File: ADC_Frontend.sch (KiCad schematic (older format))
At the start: 3 parts

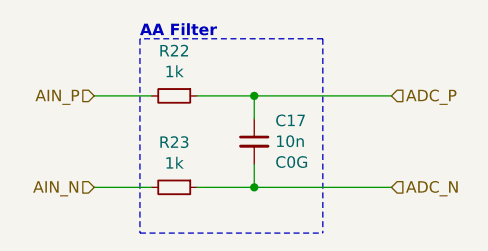
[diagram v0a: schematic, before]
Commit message: Change Sensor Connectors
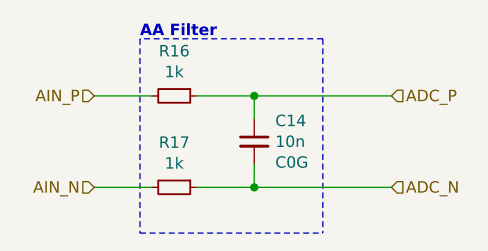
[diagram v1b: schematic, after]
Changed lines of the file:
@@
 $Descr A4 11693 8268
 encoding utf-8
-Sheet 6 17
+Sheet 3 17
 Title "Kleinvoet"
 Date "2020-06-11"
@@
 AR Path="/5EE5ECAD/5EE91C90/5EF8AB51" Ref="R20"  Part="1"
 AR Path="/5EE5ECAD/5EE9492B/5EF8AB51" Ref="R22"  Part="1"
-F 0 "R22" V 2854 2450 50  0000 C CNN
+F 0 "R16" V 2854 2450 50  0000 C CNN
 F 1 "1k" V 2945 2450 50  0000 C CNN
 F 2 "Resistor_SMD:R_0603_1608Metric_Pad1.05x0.95mm_HandSolder" H 3050 2450 50  0001 C CNN
@@
 AR Path="/5EE5ECAD/5EE91C90/5EF8AB5E" Ref="C16"  Part="1"
 AR Path="/5EE5ECAD/5EE9492B/5EF8AB5E" Ref="C17"  Part="1"
-F 0 "C17" H 3492 2741 50  0000 L CNN
+F 0 "C14" H 3492 2741 50  0000 L CNN
 F 1 "10n" H 3492 2650 50  0000 L CNN
 F 2 "Capacitor_SMD:C_0603_1608Metric_Pad1.05x0.95mm_HandSolder" H 3400 2650 50  0001 C CNN
@@
 AR Path="/5EE5ECAD/5EE91C90/5EF8D41D" Ref="R21"  Part="1"
 AR Path="/5EE5ECAD/5EE9492B/5EF8D41D" Ref="R23"  Part="1"
-F 0 "R23" V 2854 2850 50  0000 C CNN
+F 0 "R17" V 2854 2850 50  0000 C CNN
 F 1 "1k" V 2945 2850 50  0000 C CNN
 F 2 "Resistor_SMD:R_0603_1608Metric_Pad1.05x0.95mm_HandSolder" H 3050 2850 50  0001 C CNN

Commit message: PCB Layout Checkpoint
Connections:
- net ADC_N: now also C14.1, R16.1; no longer C14.2, R17.1
- net ADC_P: now also C14.2, R17.1; no longer C14.1, R16.1
- net AIN_N: now also R16.2; no longer R17.2
- net AIN_P: now also R17.2; no longer R16.2
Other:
- moved on the sheet: R22, R23
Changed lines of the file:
@@
 $Descr A4 11693 8268
 encoding utf-8
-Sheet 3 17
+Sheet 6 17
 Title "Kleinvoet"
 Date "2020-06-11"
@@
 Comment4 ""
 $EndDescr
+Wire Notes Line
+	3700 2200 2900 2200
+Text Notes 2900 2200 0    50   ~ 10
+AA Filter
+Text HLabel 2700 2850 0    50   Input ~ 0
+AIN_N
+Text HLabel 2700 2450 0    50   Input ~ 0
+AIN_P
+Text HLabel 4000 2850 2    50   Input ~ 0
+ADC_N
+Text HLabel 4000 2450 2    50   Input ~ 0
+ADC_P
+Wire Notes Line
+	2900 2200 2900 3050
+Wire Notes Line
+	3700 2200 3700 3050
+Wire Notes Line
+	2900 3050 3700 3050
+Connection ~ 3400 2850
+Wire Wire Line
+	4000 2850 3400 2850
+Connection ~ 3400 2450
+Wire Wire Line
+	4000 2450 3400 2450
+Wire Wire Line
+	2700 2450 2950 2450
+Wire Wire Line
+	2700 2850 2950 2850
+Wire Wire Line
+	3400 2450 3400 2550
+Wire Wire Line
+	3150 2450 3400 2450
+Wire Wire Line
+	3400 2850 3400 2750
+Wire Wire Line
+	3150 2850 3400 2850
 $Comp
 L Device:R_Small R?
-U 1 1 5EF8AB51
+U 1 1 5EF8D41D
 P 3050 2450
-AR Path="/5EF8AB51" Ref="R?"  Part="1"
-AR Path="/5EF7F4EB/5EF8AB51" Ref="R?"  Part="1"
-AR Path="/5EFA404B/5EF8AB51" Ref="R?"  Part="1"
-AR Path="/5EFC0F96/5EF8AB51" Ref="R?"  Part="1"
-AR Path="/5EFC2E33/5EF8AB51" Ref="R?"  Part="1"
-AR Path="/5EE5ECAD/5EE62BAF/5EF8AB51" Ref="R16"  Part="1"
-AR Path="/5EE5ECAD/5EE62BB5/5EF8AB51" Ref="R?"  Part="1"
-AR Path="/5EE5ECAD/5EE62BBB/5EF8AB51" Ref="R?"  Part="1"
-AR Path="/5EE5ECAD/5EE62BC1/5EF8AB51" Ref="R?"  Part="1"
-AR Path="/5EE5ECAD/5EE8F492/5EF8AB51" Ref="R18"  Part="1"
-AR Path="/5EE5ECAD/5EE91C90/5EF8AB51" Ref="R20"  Part="1"
-AR Path="/5EE5ECAD/5EE9492B/5EF8AB51" Ref="R22"  Part="1"
-F 0 "R16" V 2854 2450 50  0000 C CNN
+AR Path="/5EF8D41D" Ref="R?"  Part="1"
+AR Path="/5EF7F4EB/5EF8D41D" Ref="R?"  Part="1"
+AR Path="/5EFA404B/5EF8D41D" Ref="R?"  Part="1"
+AR Path="/5EFC0F96/5EF8D41D" Ref="R?"  Part="1"
+AR Path="/5EFC2E33/5EF8D41D" Ref="R?"  Part="1"
+AR Path="/5EE5ECAD/5EE62BAF/5EF8D41D" Ref="R17"  Part="1"
+AR Path="/5EE5ECAD/5EE62BB5/5EF8D41D" Ref="R?"  Part="1"
+AR Path="/5EE5ECAD/5EE62BBB/5EF8D41D" Ref="R?"  Part="1"
+AR Path="/5EE5ECAD/5EE62BC1/5EF8D41D" Ref="R?"  Part="1"
+AR Path="/5EE5ECAD/5EE8F492/5EF8D41D" Ref="R19"  Part="1"
+AR Path="/5EE5ECAD/5EE91C90/5EF8D41D" Ref="R21"  Part="1"
+AR Path="/5EE5ECAD/5EE9492B/5EF8D41D" Ref="R23"  Part="1"
+F 0 "R23" V 2854 2450 50  0000 C CNN
 F 1 "1k" V 2945 2450 50  0000 C CNN
 F 2 "Resistor_SMD:R_0603_1608Metric_Pad1.05x0.95mm_HandSolder" H 3050 2450 50  0001 C CNN
 F 3 "~" H 3050 2450 50  0001 C CNN
-F 4 "ERJ-3RBD102V" V 3050 2450 50  0001 C CNN "MPN"
-F 5 "Panasonic" V 3050 2450 50  0001 C CNN "Mfr."
+F 4 "ERJ-3RBD102V" H 3050 2450 50  0001 C CNN "MPN"
+F 5 "Panasonic" H 3050 2450 50  0001 C CNN "Mfr."
 	1    3050 2450
-	0    1    1    0
+	0    1    -1   0
 $EndComp
 $Comp
@@
 AR Path="/5EE5ECAD/5EE91C90/5EF8AB5E" Ref="C16"  Part="1"
 AR Path="/5EE5ECAD/5EE9492B/5EF8AB5E" Ref="C17"  Part="1"
-F 0 "C14" H 3492 2741 50  0000 L CNN
+F 0 "C17" H 3492 2741 50  0000 L CNN
 F 1 "10n" H 3492 2650 50  0000 L CNN
 F 2 "Capacitor_SMD:C_0603_1608Metric_Pad1.05x0.95mm_HandSolder" H 3400 2650 50  0001 C CNN
@@
 F 6 "KEMET" H 3400 2650 50  0001 C CNN "Mfr."
 	1    3400 2650
-	1    0    0    -1
+	1    0    0    1
 $EndComp
 $Comp
 L Device:R_Small R?
-U 1 1 5EF8D41D
+U 1 1 5EF8AB51
 P 3050 2850
-AR Path="/5EF8D41D" Ref="R?"  Part="1"
-AR Path="/5EF7F4EB/5EF8D41D" Ref="R?"  Part="1"
-AR Path="/5EFA404B/5EF8D41D" Ref="R?"  Part="1"
-AR Path="/5EFC0F96/5EF8D41D" Ref="R?"  Part="1"
-AR Path="/5EFC2E33/5EF8D41D" Ref="R?"  Part="1"
-AR Path="/5EE5ECAD/5EE62BAF/5EF8D41D" Ref="R17"  Part="1"
-AR Path="/5EE5ECAD/5EE62BB5/5EF8D41D" Ref="R?"  Part="1"
-AR Path="/5EE5ECAD/5EE62BBB/5EF8D41D" Ref="R?"  Part="1"
-AR Path="/5EE5ECAD/5EE62BC1/5EF8D41D" Ref="R?"  Part="1"
-AR Path="/5EE5ECAD/5EE8F492/5EF8D41D" Ref="R19"  Part="1"
-AR Path="/5EE5ECAD/5EE91C90/5EF8D41D" Ref="R21"  Part="1"
-AR Path="/5EE5ECAD/5EE9492B/5EF8D41D" Ref="R23"  Part="1"
-F 0 "R17" V 2854 2850 50  0000 C CNN
+AR Path="/5EF8AB51" Ref="R?"  Part="1"
+AR Path="/5EF7F4EB/5EF8AB51" Ref="R?"  Part="1"
+AR Path="/5EFA404B/5EF8AB51" Ref="R?"  Part="1"
+AR Path="/5EFC0F96/5EF8AB51" Ref="R?"  Part="1"
+AR Path="/5EFC2E33/5EF8AB51" Ref="R?"  Part="1"
+AR Path="/5EE5ECAD/5EE62BAF/5EF8AB51" Ref="R16"  Part="1"
+AR Path="/5EE5ECAD/5EE62BB5/5EF8AB51" Ref="R?"  Part="1"
+AR Path="/5EE5ECAD/5EE62BBB/5EF8AB51" Ref="R?"  Part="1"
+AR Path="/5EE5ECAD/5EE62BC1/5EF8AB51" Ref="R?"  Part="1"
+AR Path="/5EE5ECAD/5EE8F492/5EF8AB51" Ref="R18"  Part="1"
+AR Path="/5EE5ECAD/5EE91C90/5EF8AB51" Ref="R20"  Part="1"
+AR Path="/5EE5ECAD/5EE9492B/5EF8AB51" Ref="R22"  Part="1"
+F 0 "R22" V 2854 2850 50  0000 C CNN
 F 1 "1k" V 2945 2850 50  0000 C CNN
 F 2 "Resistor_SMD:R_0603_1608Metric_Pad1.05x0.95mm_HandSolder" H 3050 2850 50  0001 C CNN
 F 3 "~" H 3050 2850 50  0001 C CNN
-F 4 "ERJ-3RBD102V" H 3050 2850 50  0001 C CNN "MPN"
-F 5 "Panasonic" H 3050 2850 50  0001 C CNN "Mfr."
+F 4 "ERJ-3RBD102V" V 3050 2850 50  0001 C CNN "MPN"
+F 5 "Panasonic" V 3050 2850 50  0001 C CNN "Mfr."
 	1    3050 2850
-	0    1    1    0
+	0    1    -1   0
 $EndComp
-Wire Wire Line
-	3150 2450 3400 2450
-Wire Wire Line
-	3400 2450 3400 2550
-Wire Wire Line
-	3150 2850 3400 2850
-Wire Wire Line
-	3400 2850 3400 2750
-Wire Wire Line
-	2700 2450 2950 2450
-Wire Wire Line
-	2700 2850 2950 2850
-Wire Wire Line
-	4000 2850 3400 2850
-Connection ~ 3400 2850
-Wire Wire Line
-	4000 2450 3400 2450
-Connection ~ 3400 2450
-Wire Notes Line
-	2900 3050 3700 3050
-Wire Notes Line
-	3700 2200 2900 2200
-Text Notes 2900 2200 0    50   ~ 10
-AA Filter
-Wire Notes Line
-	3700 2200 3700 3050
-Wire Notes Line
-	2900 2200 2900 3050
-Text HLabel 4000 2450 2    50   Input ~ 0
-ADC_P
-Text HLabel 4000 2850 2    50   Input ~ 0
-ADC_N
-Text HLabel 2700 2450 0    50   Input ~ 0
-AIN_P
-Text HLabel 2700 2850 0    50   Input ~ 0
-AIN_N
 $EndSCHEMATC

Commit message: Major Commit with Final PCB Design
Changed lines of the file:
@@
 $Descr A4 11693 8268
 encoding utf-8
-Sheet 6 17
+Sheet 3 17
 Title "Kleinvoet"
 Date "2020-06-11"
@@
 AR Path="/5EE5ECAD/5EE91C90/5EF8D41D" Ref="R21"  Part="1"
 AR Path="/5EE5ECAD/5EE9492B/5EF8D41D" Ref="R23"  Part="1"
-F 0 "R23" V 2854 2450 50  0000 C CNN
+F 0 "R17" V 2854 2450 50  0000 C CNN
 F 1 "1k" V 2945 2450 50  0000 C CNN
 F 2 "Resistor_SMD:R_0603_1608Metric_Pad1.05x0.95mm_HandSolder" H 3050 2450 50  0001 C CNN
@@
 AR Path="/5EE5ECAD/5EE91C90/5EF8AB5E" Ref="C16"  Part="1"
 AR Path="/5EE5ECAD/5EE9492B/5EF8AB5E" Ref="C17"  Part="1"
-F 0 "C17" H 3492 2741 50  0000 L CNN
+F 0 "C14" H 3492 2741 50  0000 L CNN
 F 1 "10n" H 3492 2650 50  0000 L CNN
 F 2 "Capacitor_SMD:C_0603_1608Metric_Pad1.05x0.95mm_HandSolder" H 3400 2650 50  0001 C CNN
@@
 AR Path="/5EE5ECAD/5EE91C90/5EF8AB51" Ref="R20"  Part="1"
 AR Path="/5EE5ECAD/5EE9492B/5EF8AB51" Ref="R22"  Part="1"
-F 0 "R22" V 2854 2850 50  0000 C CNN
+F 0 "R16" V 2854 2850 50  0000 C CNN
 F 1 "1k" V 2945 2850 50  0000 C CNN
 F 2 "Resistor_SMD:R_0603_1608Metric_Pad1.05x0.95mm_HandSolder" H 3050 2850 50  0001 C CNN

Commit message: Misc. TODOs
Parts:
- C14: footprint Capacitor_SMD:C_0603_1608Metric_Pad1.05x0.95mm_HandSolder -> Capacitor_SMD:C_0603_1608Metric_Pad1.08x0.95mm_HandSolder
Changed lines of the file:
@@
 F 0 "C14" H 3492 2741 50  0000 L CNN
 F 1 "10n" H 3492 2650 50  0000 L CNN
-F 2 "Capacitor_SMD:C_0603_1608Metric_Pad1.05x0.95mm_HandSolder" H 3400 2650 50  0001 C CNN
+F 2 "Capacitor_SMD:C_0603_1608Metric_Pad1.08x0.95mm_HandSolder" H 3400 2650 50  0001 C CNN
 F 3 "~" H 3400 2650 50  0001 C CNN
 F 4 "C0G" H 3492 2559 50  0000 L CNN "Notes"

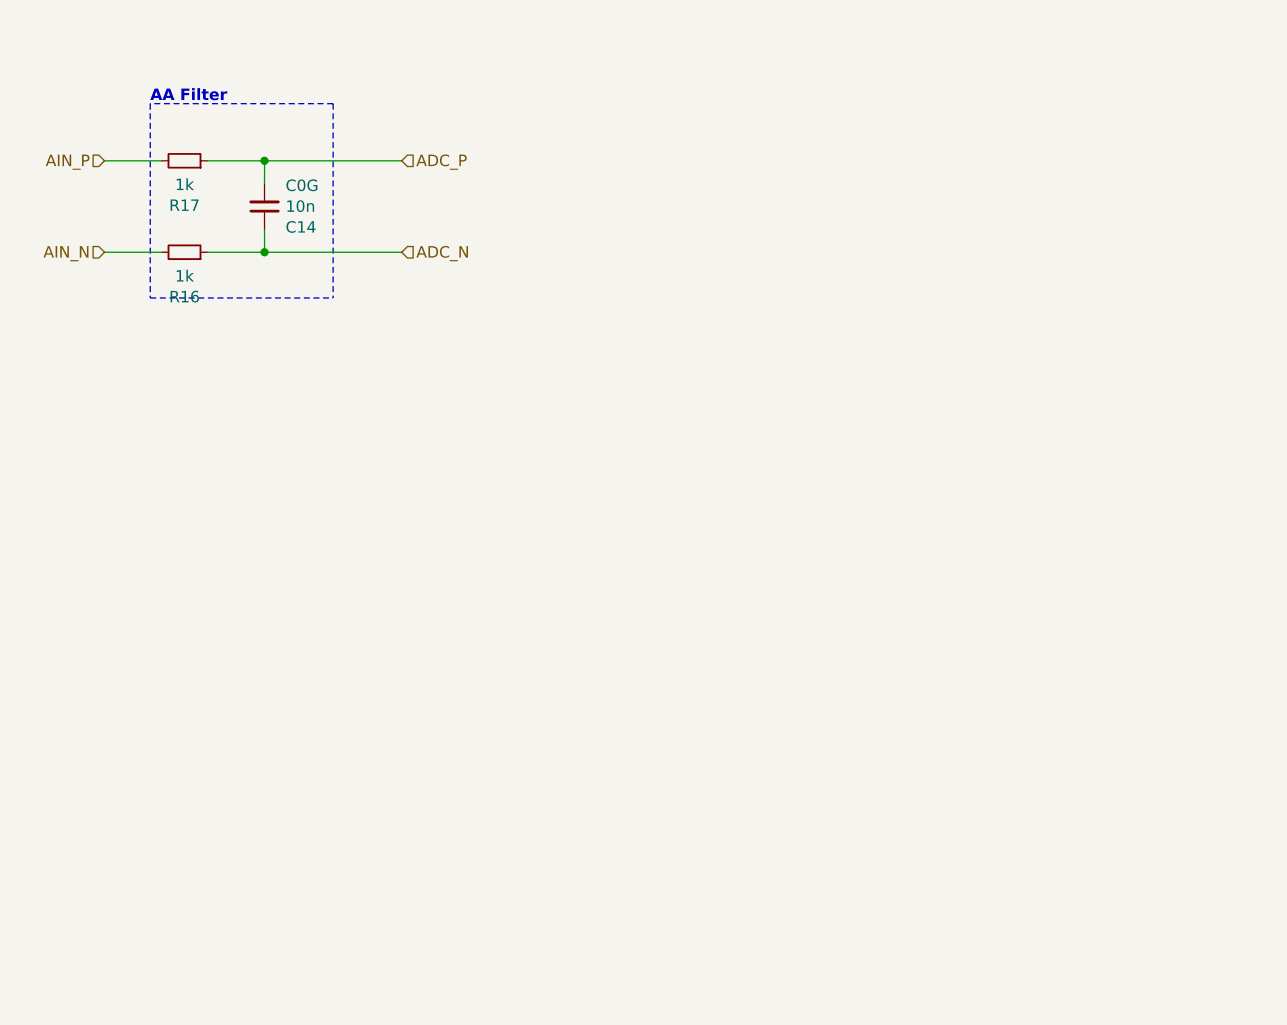
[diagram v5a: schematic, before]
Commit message: New ADC board layout
Merge feature/kv-new-adc

Squashed commit of the following:
===============================================

commit d560af3129baffdc71a13a7fa7beda6d7e4b1bbe
Author: CM Geldenhuys <20198329@sun.ac.za>
Date:   Mon Nov 2 10:16:05 2020 +0200

    Change board layout

commit e0e102b1b715915958904bd07514080422fcc802
Author: CM Geldenhuys <20198329@sun.ac.za>
Date:   Mon Nov 2 08:42:49 2020 +0200

    Route ADC rst

commit dbc5adba55d665b163eedfb4150514fe2b5b8ec8
Author: CM Geldenhuys <20198329@sun.ac.za>
Date:   Mon Nov 2 08:37:27 2020 +0200

    Fix GPS conn.

commit 0f139c20ac4bbbbfd2ab5507f187a5ddf70be7a1
Author: CM Geldenhuys <20198329@sun.ac.za>
Date:   Mon Nov 2 08:23:01 2020 +0200

    Route USR BTN

commit f6bd16c8e79a9fc3047a82e3e1abb388a579a1e4
Author: CM Geldenhuys <20198329@sun.ac.za>
Date:   Sun Nov 1 07:41:20 2020 +0200

    Route GPS Conn

commit 016e6e7ba1ce602e3233b00102ced6621a380f78
Author: CM Geldenhuys <20198329@sun.ac.za>
Date:   Fri Oct 30 17:31:13 2020 +0200

    Route Misc.

commit 6a809ae2e129821f12cca4ec3806ebf69337c268
Author: CM Geldenhuys <20198329@sun.ac.za>
Date:   Fri Oct 30 11:40:29 2020 +0200

    (WIP) SD config

commit b5d79f248cd283a71c5ab746a4afc4eb96850216
Author: CM Geldenhuys <20198329@sun.ac.za>
Date:   Fri Oct 30 11:24:56 2020 +0200

    Route ST-Link

commit dba35a7554c0c60ddd581dd4b7cbdf28445f26a1
Author: CM Geldenhuys <20198329@sun.ac.za>
Date:   Fri Oct 30 11:03:44 2020 +0200

    Route out GND planes

commit ee78e0f947a8edc358d3e2ec17c7ddf8f87e82dd
Author: CM Geldenhuys <20198329@sun.ac.za>
Date:   Thu Oct 29 16:17:03 2020 +0200

    Change ST-LINk loc.

commit b281a3fe16ed9d80db1964422c72eaf6acbfd9f3
Author: CM Geldenhuys <20198329@sun.ac.za>
Date:   Thu Oct 29 15:43:37 2020 +0200

    Major layout update

commit 655eae6cd0c7e79d683f16c4706ab989a6952fc5
Author: CM Geldenhuys <20198329@sun.ac.za>
Date:   Thu Oct 29 12:05:26 2020 +0200

    Route analog section

commit 0aa4140e89fcb36b0e9f339e25cad0a47a5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
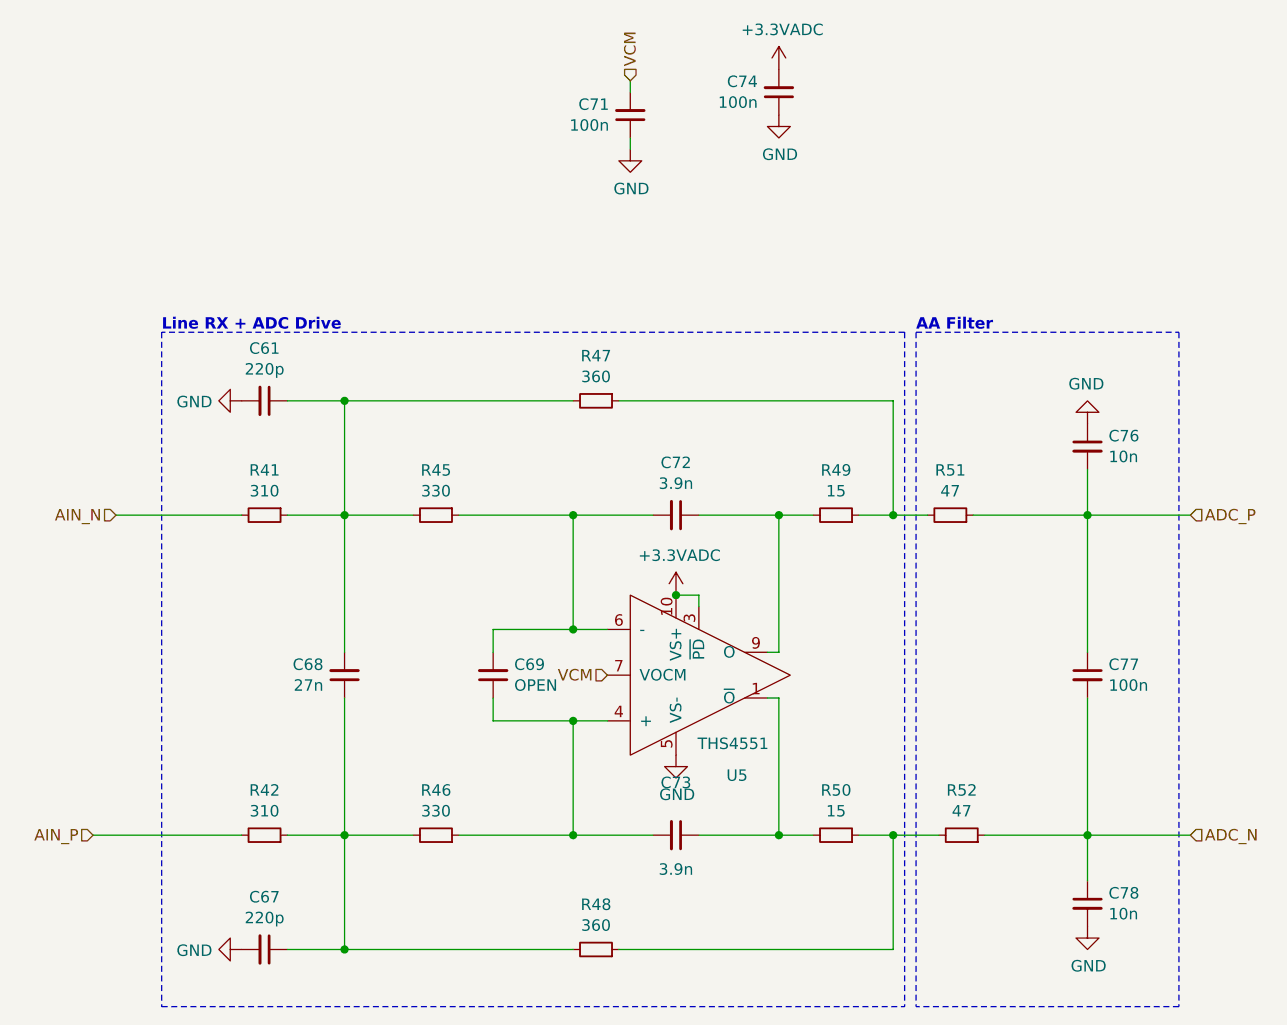
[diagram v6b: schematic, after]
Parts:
- removed C14: 10n, Capacitor_SMD:C_0603_1608Metric_Pad1.08x0.95mm_HandSolder, symbol Device:C_Small
- removed R16: 1k, Resistor_SMD:R_0603_1608Metric_Pad1.05x0.95mm_HandSolder, symbol Device:R_Small
- added C26, C27: 220p, Capacitor_SMD:C_0603_1608Metric_Pad1.08x0.95mm_HandSolder, symbol Device:C_Small
- added C34: 27n, Capacitor_SMD:C_0603_1608Metric_Pad1.08x0.95mm_HandSolder, symbol Device:C_Small
- added C35: OPEN, Capacitor_SMD:C_0603_1608Metric_Pad1.08x0.95mm_HandSolder, symbol Device:C_Small
- added C37, C40, C43: 100n, Capacitor_SMD:C_0603_1608Metric_Pad1.08x0.95mm_HandSolder, symbol Device:C_Small
- added C38, C39: 3.9n, Capacitor_SMD:C_0603_1608Metric_Pad1.08x0.95mm_HandSolder, symbol Device:C_Small
- added C42, C44: 10n, Capacitor_SMD:C_0603_1608Metric_Pad1.08x0.95mm_HandSolder, symbol Device:C_Small
- added R18: 310, Resistor_SMD:R_0603_1608Metric_Pad0.98x0.95mm_HandSolder, symbol Device:R_Small
- added R21, R22: 330, Resistor_SMD:R_0603_1608Metric_Pad0.98x0.95mm_HandSolder, symbol Device:R_Small
- added R23, R24: 360, Resistor_SMD:R_0603_1608Metric_Pad0.98x0.95mm_HandSolder, symbol Device:R_Small
- added R25, R26: 15, Resistor_SMD:R_0603_1608Metric_Pad0.98x0.95mm_HandSolder, symbol Device:R_Small
- added R27, R28: 47, Resistor_SMD:R_0603_1608Metric_Pad0.98x0.95mm_HandSolder, symbol Device:R_Small
- added U3: THS4551, grootvoet:WQFN-10_RUN, symbol grootvoet:THS4551
- R17: value 1k -> 310; footprint Resistor_SMD:R_0603_1608Metric_Pad1.05x0.95mm_HandSolder -> Resistor_SMD:R_0603_1608Metric_Pad0.98x0.95mm_HandSolder; MPN ERJ-3RBD102V -> (none); Mfr. Panasonic -> (none)
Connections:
- net ADC_N: now also C43.2, C44.1, R28.1
- net ADC_P: now also C42.2, C43.1, R27.1; no longer R17.1
- net AIN_N: now also R17.2
- net AIN_P: now also R18.2; no longer R17.2
- new net: C26.1, C34.2, R17.1, R21.2, R23.2
- new net: C35.2, C38.2, R21.1, U3.6 (-)
- new net: R23.1, R25.1, R27.2
- new net: C38.1, R25.2, U3.9 (O)
- new net: C27.1, C34.1, R18.1, R22.2, R24.2
- new net: C35.1, C39.2, R22.1, U3.4 (+)
- new net: R24.1, R26.1, R28.2
- new net: C39.1, R26.2, U3.1 (~O)
- new net +3.3VADC: C40.2, U3.10 (VS+), U3.3 (~PD)
- new net GND: C26.2, C27.2, C37.1, C40.1, C42.1, C44.2, U3.5 (VS-)
- new net VCM: C37.2, U3.7 (VOCM)
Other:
- note added: "Line RX + ADC Drive"
